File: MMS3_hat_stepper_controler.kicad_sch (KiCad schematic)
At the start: 6 parts

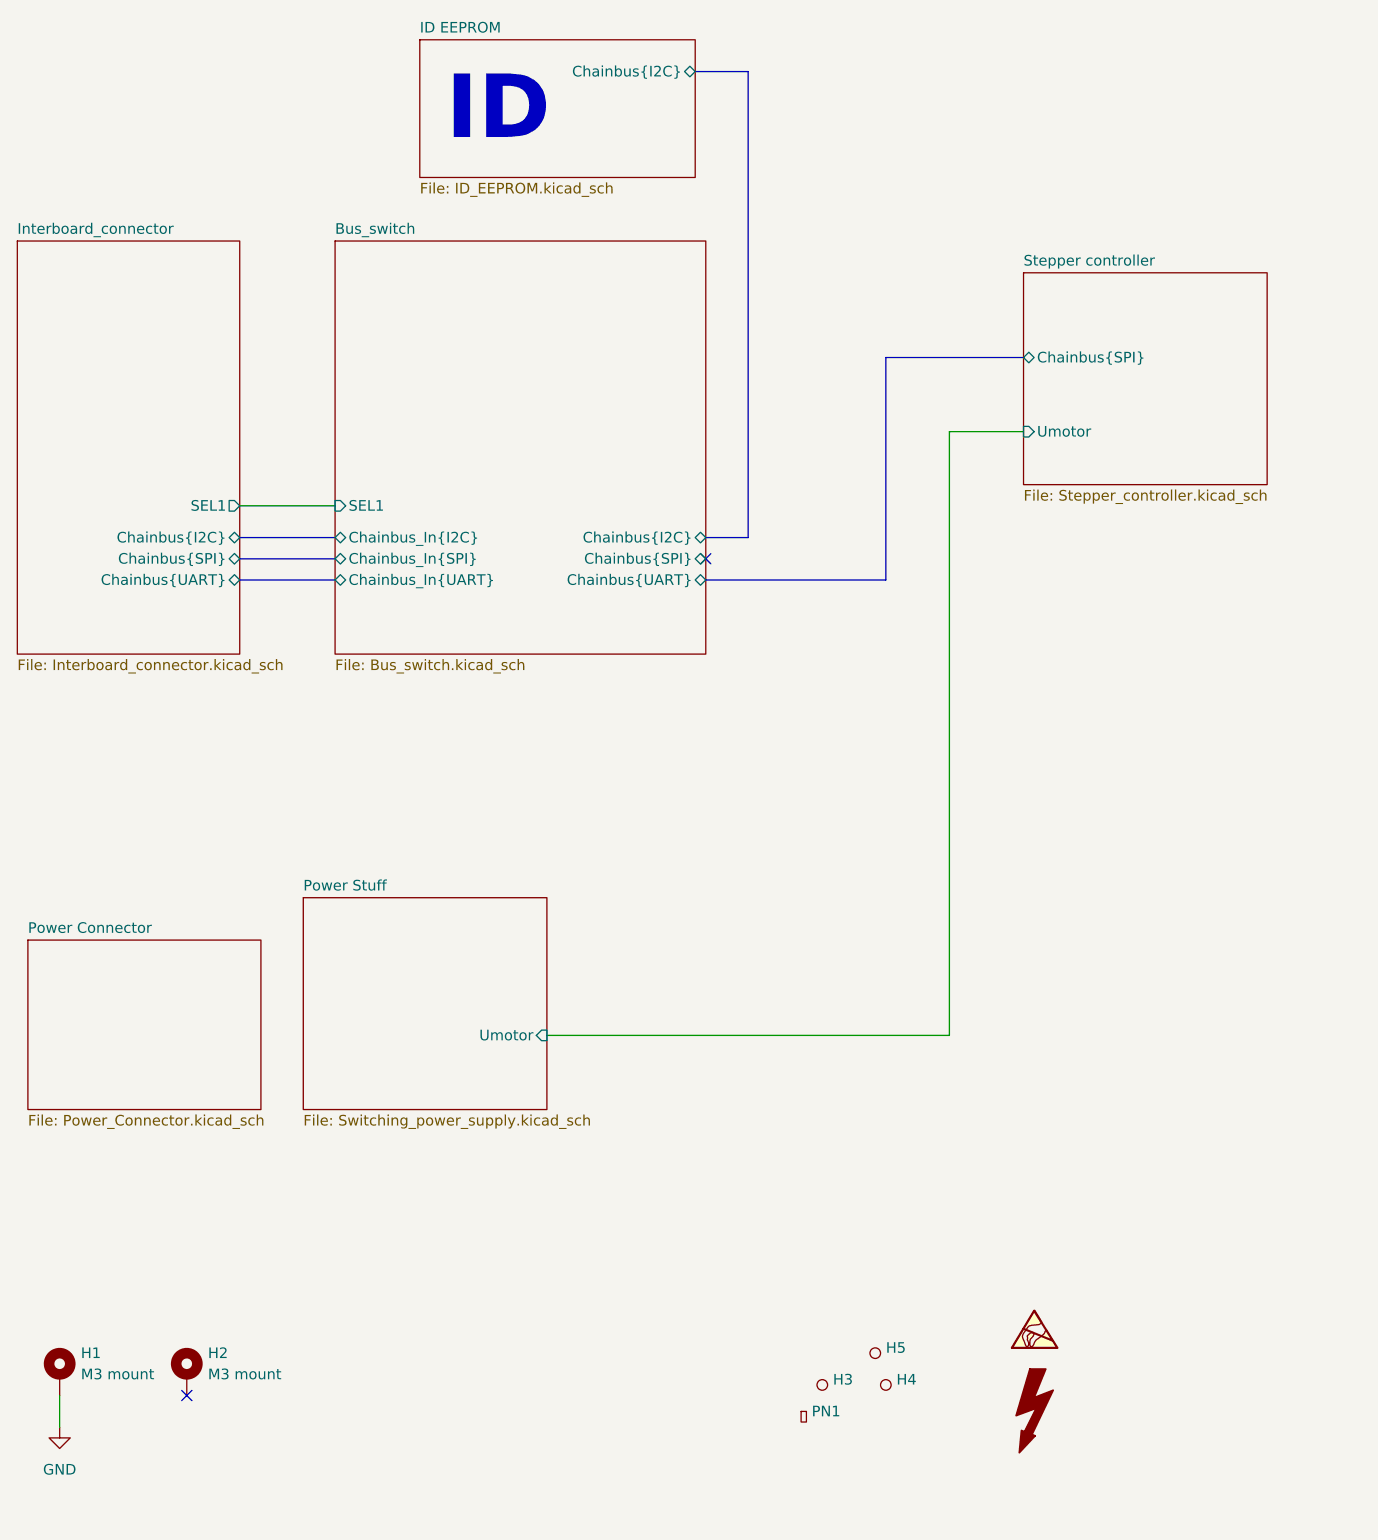
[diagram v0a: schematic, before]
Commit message: finished schematic (without some part numbers)
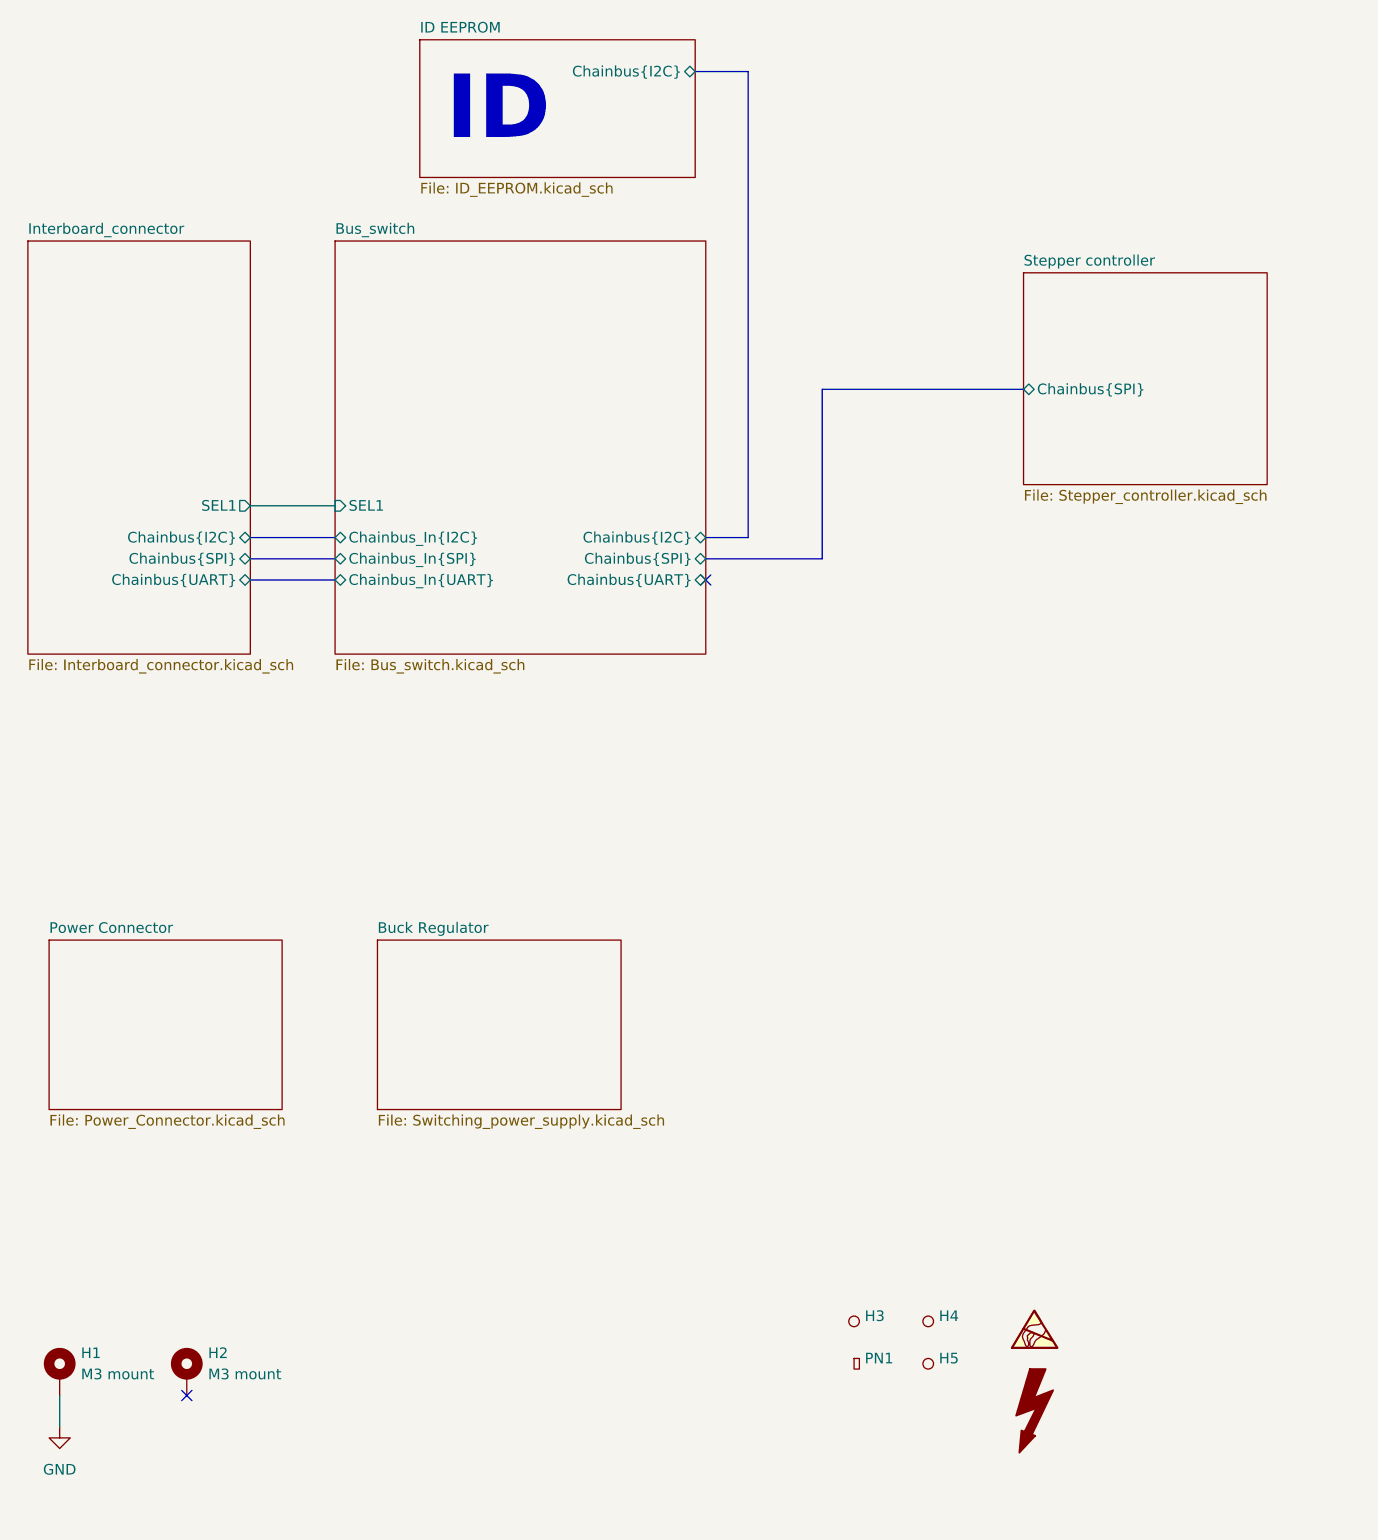
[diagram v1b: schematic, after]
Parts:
- renumbered H5 to H4, H4 to H5
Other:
- sheet Power Stuff renamed Buck Regulator
- sheet Buck Regulator ports: added none; removed Umotor
- sheet Stepper controller ports: added none; removed Umotor
- title: MMS2 Hat template small (Change Me) -> MMS3 Stepper Controler
- moved on the sheet: H3, H4, H5, PN1

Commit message: revision
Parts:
- added H3, H4: M3 mount, MountingHole:MountingHole_2.7mm_M2.5_DIN965, symbol Mechanical:MountingHole_Pad
- H1: footprint MountingHole:MountingHole_3.2mm_M3_DIN965_Pad -> MountingHole:MountingHole_2.7mm_M2.5_DIN965_Pad_TopOnly
- H2: footprint MountingHole:MountingHole_3.2mm_M3_DIN965_Pad -> MountingHole:MountingHole_2.7mm_M2.5_DIN965
- renumbered H3 to H5, H4 to H6, H5 to H7
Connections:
- no-connect marks 2 -> 4
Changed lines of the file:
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@@
 	)
 	(no_connect
+		(at 68.58 180.34)
+	)
+	(no_connect
 		(at 34.29 180.34)
 	)
+	(no_connect
+		(at 53.34 180.34)
+	)
 	(wire
 		(pts
@@
 		(dnp no)
 		(fields_autoplaced yes)
-		(property "Reference" "H3"
+		(property "Reference" "H5"
 			(at 115.57 170.8149 0)
 			(effects
@@
 			(project "MMS2_hat_template_small"
 				(path "/6596548a-44e0-46d8-8624-fd71cf4a3e17"
-					(reference "H3")
+					(reference "H5")
 					(unit 1)
 				)
@@
 	)
 	(symbol
+		(lib_id "Mechanical:MountingHole_Pad")
+		(at 53.34 177.8 0)
+		(unit 1)
+		(exclude_from_sim yes)
+		(in_bom no)
+		(on_board yes)
+		(dnp no)
+		(fields_autoplaced yes)
+		(property "Reference" "H3"
+			(at 55.88 175.26 0)
+			(effects
+				(font
+					(size 1.27 1.27)
+				)
+				(justify left)
+			)
+		)
+		(property "Value" "M3 mount"
+			(at 55.88 177.8 0)
+			(effects
+				(font
+					(size 1.27 1.27)
+				)
+				(justify left)
+			)
+		)
+		(property "Footprint" "MountingHole:MountingHole_2.7mm_M2.5_DIN965"
+			(at 53.34 177.8 0)
+			(effects
+				(font
+					(size 1.27 1.27)
+				)
+				(hide yes)
+			)
+		)
+		(property "Datasheet" "~"
+			(at 53.34 177.8 0)
+			(effects
+				(font
+					(size 1.27 1.27)
+				)
+				(hide yes)
+			)
+		)
+		(property "Description" "Mounting Hole with connection"
+			(at 53.34 177.8 0)
+			(effects
+				(font
+					(size 1.27 1.27)
+				)
+				(hide yes)
+			)
+		)
+		(pin "1"
+		)
+		(instances
+			(project "MMS3_hat_stepper_controler"
+				(path "/6596548a-44e0-46d8-8624-fd71cf4a3e17"
+					(reference "H3")
+					(unit 1)
+				)
+			)
+		)
+	)
+	(symbol
 		(lib_id "PCM_JLCPCB-Manufacturing:Tooling Hole, PCM_JLCPCB, 1.152mm")
 		(at 123.19 171.45 0)
@@
 		(dnp no)
 		(fields_autoplaced yes)
-		(property "Reference" "H4"
+		(property "Reference" "H6"
 			(at 124.46 170.8149 0)
 			(effects
@@
 			(project "MMS2_hat_template_small"
 				(path "/6596548a-44e0-46d8-8624-fd71cf4a3e17"
+					(reference "H6")
+					(unit 1)
+				)
+			)
+		)
+	)
+	(symbol
+		(lib_id "Mechanical:MountingHole_Pad")
+		(at 68.58 177.8 0)
+		(unit 1)
+		(exclude_from_sim yes)
+		(in_bom no)
+		(on_board yes)
+		(dnp no)
+		(fields_autoplaced yes)
+		(property "Reference" "H4"
+			(at 71.12 175.26 0)
+			(effects
+				(font
+					(size 1.27 1.27)
+				)
+				(justify left)
+			)
+		)
+		(property "Value" "M3 mount"
+			(at 71.12 177.8 0)
+			(effects
+				(font
+					(size 1.27 1.27)
+				)
+				(justify left)
+			)
+		)
+		(property "Footprint" "MountingHole:MountingHole_2.7mm_M2.5_DIN965"
+			(at 68.58 177.8 0)
+			(effects
+				(font
+					(size 1.27 1.27)
+				)
+				(hide yes)
+			)
+		)
+		(property "Datasheet" "~"
+			(at 68.58 177.8 0)
+			(effects
+				(font
+					(size 1.27 1.27)
+				)
+				(hide yes)
+			)
+		)
+		(property "Description" "Mounting Hole with connection"
+			(at 68.58 177.8 0)
+			(effects
+				(font
+					(size 1.27 1.27)
+				)
+				(hide yes)
+			)
+		)
+		(pin "1"
+		)
+		(instances
+			(project "MMS3_hat_stepper_controler"
+				(path "/6596548a-44e0-46d8-8624-fd71cf4a3e17"
 					(reference "H4")
 					(unit 1)
@@
 		(dnp no)
 		(fields_autoplaced yes)
-		(property "Reference" "H5"
+		(property "Reference" "H7"
 			(at 124.46 175.8949 0)
 			(effects
@@
 			(project "MMS2_hat_template_small"
 				(path "/6596548a-44e0-46d8-8624-fd71cf4a3e17"
-					(reference "H5")
+					(reference "H7")
 					(unit 1)
 				)
@@
 			)
 		)
-		(property "Footprint" "MountingHole:MountingHole_3.2mm_M3_DIN965_Pad"
+		(property "Footprint" "MountingHole:MountingHole_2.7mm_M2.5_DIN965"
 			(at 34.29 177.8 0)
 			(effects
@@
 			)
 		)
-		(property "Footprint" "MountingHole:MountingHole_3.2mm_M3_DIN965_Pad"
+		(property "Footprint" "MountingHole:MountingHole_2.7mm_M2.5_DIN965_Pad_TopOnly"
 			(at 19.05 177.8 0)
 			(effects

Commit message: second component placement
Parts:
- removed H2, H3, H4: M3 mount, MountingHole:MountingHole_2.7mm_M2.5_DIN965, symbol Mechanical:MountingHole_Pad
- added H2, H3, H4, H5, H6: M2.5 mount, MountingHole:MountingHole_2.7mm_M2.5, symbol Mechanical:MountingHole
- H1: value M3 mount -> M2.5 Mount
- renumbered H5 to H7, H6 to H8, H7 to H9
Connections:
- no-connect marks 4 -> 1
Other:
- moved on the sheet: H7, H8, H9, PN1

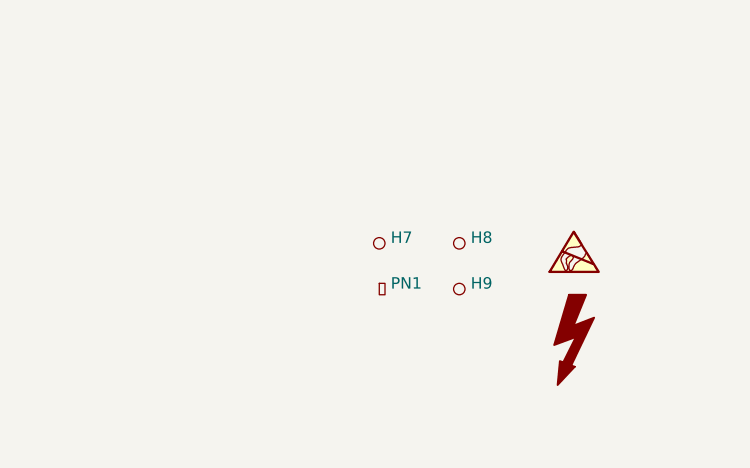
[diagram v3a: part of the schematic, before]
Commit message: added pinout on silkscreen
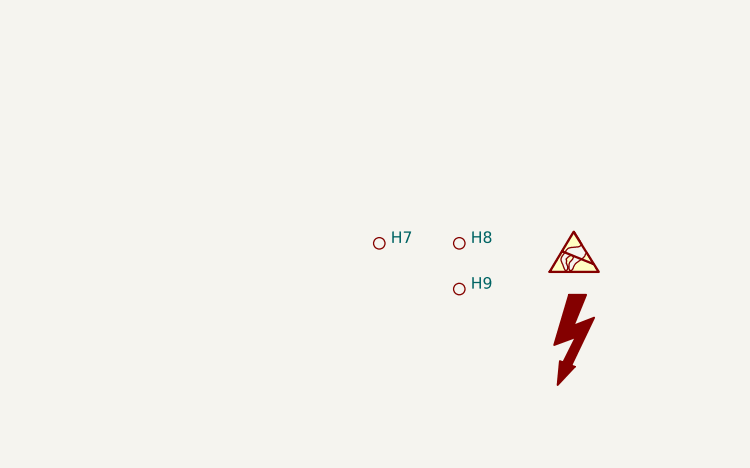
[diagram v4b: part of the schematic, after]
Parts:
- removed PN1: ~, PCM_JLCPCB:Part_Num_JLCPCB, symbol PCM_JLCPCB-Manufacturing:Part Number, PCM_JLCPCB, 0.8x0.15mm
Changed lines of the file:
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@@
-	)
-	(symbol
-		(lib_id "PCM_JLCPCB-Manufacturing:Part Number, PCM_JLCPCB, 0.8x0.15mm")
-		(at 135.89 177.8 0)
-		(unit 1)
-		(exclude_from_sim no)
-		(in_bom yes)
-		(on_board yes)
-		(dnp no)
-		(fields_autoplaced yes)
-		(property "Reference" "PN1"
-			(at 137.16 177.1649 0)
-			(effects
-				(font
-					(size 1.27 1.27)
-				)
-				(justify left)
-			)
-		)
-		(property "Value" "~"
-			(at 137.16 179.07 0)
-			(effects
-				(font
-					(size 1.27 1.27)
-				)
-				(justify left)
-			)
-		)
-		(property "Footprint" "PCM_JLCPCB:Part_Num_JLCPCB"
-			(at 135.89 177.8 0)
-			(effects
-				(font
-					(size 1.27 1.27)
-				)
-				(hide yes)
-			)
-		)
-		(property "Datasheet" "https://jlcpcb.com/help/article/How-to-remove-order-number-from-your-PCB"
-			(at 135.89 177.8 0)
-			(effects
-				(font
-					(size 1.27 1.27)
-				)
-				(hide yes)
-			)
-		)
-		(property "Description" "To indicate the location, simply add the text \"JLCJLCJLCJLC\" to the silk layer and select the \"Specify a location\" option when placing your order. Please note that if this option is not chosen, we may not notice that you have added the text.   Note: Use only \"JLCJLCJLCJLC\" without any additional characters. The font size should be larger than 0.8mm in height and 0.15mm in width."
-			(at 135.89 177.8 0)
-			(effects
-				(font
-					(size 1.27 1.27)
-				)
-				(hide yes)
-			)
-		)
-		(property "Sim.Device" ""
-			(at 135.89 177.8 0)
-			(effects
-				(font
-					(size 1.27 1.27)
-				)
-				(hide yes)
-			)
-		)
-		(instances
-			(project "MMS2_hat_template_small"
-				(path "/6596548a-44e0-46d8-8624-fd71cf4a3e17"
-					(reference "PN1")
-					(unit 1)
-				)
-			)
-		)
 	)
 	(symbol

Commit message: moved the converter, to the long side this time
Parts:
- H7, H8, H9: value ~ -> (none)
